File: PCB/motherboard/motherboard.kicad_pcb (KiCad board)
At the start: 2 copper layers, 68 parts, among them U1 TPS54140ADGQR, U2 PTPS259830LNRGER, U3 AP2112K-3.3TRG1, U4 NUCLEO-L432KC, U5 TXS0104EPWR, U6 LM74700QDBVTQ1, U7 25LC256-I/SN, U8 AM26LS32ACDR, U9 TL431D

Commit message: added last footprint on sch
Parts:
- added C26: DNP, Capacitor_SMD:C_1206_3216Metric_Pad1.33x1.80mm_HandSolder, F.Cu at (139.1, 117.9)
- added C27: 100n, Capacitor_SMD:C_1206_3216Metric_Pad1.33x1.80mm_HandSolder, F.Cu at (172.9, 46.7)
- added C28: 100n, Capacitor_SMD:C_1206_3216Metric_Pad1.33x1.80mm_HandSolder, F.Cu at (172.9, 50.0)
- added C29: 100n, Capacitor_SMD:C_1206_3216Metric_Pad1.33x1.80mm_HandSolder, F.Cu at (172.9, 53.4)
- added C30: 100n, Capacitor_SMD:C_1206_3216Metric_Pad1.33x1.80mm_HandSolder, F.Cu at (172.9, 56.7)
- added C31: 100n, Capacitor_SMD:C_1206_3216Metric_Pad1.33x1.80mm_HandSolder, F.Cu at (172.9, 60.1)
- added C32: 100n, Capacitor_SMD:C_1206_3216Metric_Pad1.33x1.80mm_HandSolder, F.Cu at (172.9, 63.4)
- added D1: 26V, diodes:SMB_L4.3-W3.6-LS5.4-BI, F.Cu at (146.5, 137.1)
- added J1: Conn_01x04, TerminalBlock_Phoenix:TerminalBlock_Phoenix_MPT-0,5-4-2.54_1x04_P2.54mm_Horizontal, F.Cu at (111.9, 127.3)
- added J10: Screw_Terminal_01x03, TerminalBlock_Phoenix:TerminalBlock_Phoenix_MPT-0,5-3-2.54_1x03_P2.54mm_Horizontal, F.Cu at (84.0, 128.0)
- added J11: Conn_01x05, TerminalBlock_Phoenix:TerminalBlock_Phoenix_MPT-0,5-5-2.54_1x05_P2.54mm_Horizontal, F.Cu at (94.2, 144.3)
- added J12: Conn_01x11, TerminalBlock_Phoenix:TerminalBlock_Phoenix_MPT-0,5-11-2.54_1x11_P2.54mm_Horizontal, F.Cu at (94.2, 110.3)
- added J13: Conn_01x03, TerminalBlock_Phoenix:TerminalBlock_Phoenix_MPT-0,5-3-2.54_1x03_P2.54mm_Horizontal, F.Cu at (84.0, 136.9)
- added J2: Conn_01x06, TerminalBlock_Phoenix:TerminalBlock_Phoenix_MPT-0,5-6-2.54_1x06_P2.54mm_Horizontal, F.Cu at (94.2, 127.3)
- added J3: Conn_01x08, TerminalBlock_Phoenix:TerminalBlock_Phoenix_MPT-0,5-8-2.54_1x08_P2.54mm_Horizontal, F.Cu at (94.2, 118.8)
- added J4: Conn_01x04, TerminalBlock_Phoenix:TerminalBlock_Phoenix_MPT-0,5-4-2.54_1x04_P2.54mm_Horizontal, F.Cu at (111.9, 135.8)
- added J5: Conn_01x03, TerminalBlock_Phoenix:TerminalBlock_Phoenix_MPT-0,5-3-2.54_1x03_P2.54mm_Horizontal, F.Cu at (84.0, 110.3)
- added J6: Conn_01x03, TerminalBlock_Phoenix:TerminalBlock_Phoenix_MPT-0,5-3-2.54_1x03_P2.54mm_Horizontal, F.Cu at (84.0, 119.2)
- added J8: Conn_01x06, TerminalBlock_Phoenix:TerminalBlock_Phoenix_MPT-0,5-6-2.54_1x06_P2.54mm_Horizontal, F.Cu at (94.2, 135.8)
- added J9: Conn_01x02, TerminalBlock_Phoenix:TerminalBlock_Phoenix_MKDS-3-2-5.08_1x02_P5.08mm_Horizontal, F.Cu at (110.4, 147.1)
- added L1: 47u, inductors:IND-SMD_L7.3-W6.8, F.Cu at (147.1, 130.2)
- added L2: 22uH, inductors:IND-SMD_L17.0-W17.0_YSPIA1770-100M, F.Cu at (92.2, 54.3)
- added L3: 22uH, inductors:IND-SMD_L17.0-W17.0_YSPIA1770-100M, F.Cu at (92.2, 72.9)
- added L4: 22uH, inductors:IND-SMD_L17.0-W17.0_YSPIA1770-100M, F.Cu at (92.2, 91.6)
- added Q1: NMOS, transistors:PG-TDSON-8_L5.0-W6.0-P1.27-BL-EP, F.Cu at (133.1, 88.5)
- added Q2: PMOS, transistors:DFN-8_L5.7-W4.9-P1.27-LS6.1-BL, F.Cu at (140.2, 88.4)
- added Q3: NMOS, transistors:SOT-23-3_L2.9-W1.3-P1.90-LS2.4-BR, F.Cu at (172.3, 92.1)
- added R28: 25 Ohm, resistors:TO-220-2_L10.1-W4.5-P5.08-L, F.Cu at (135.6, 80.7)
- added R29: 105k, Resistor_SMD:R_1206_3216Metric_Pad1.30x1.75mm_HandSolder, F.Cu at (157.0, 117.7)
- added R30: 6k49, Resistor_SMD:R_1206_3216Metric_Pad1.30x1.75mm_HandSolder, F.Cu at (157.0, 121.1)
- added R31: 10k, Resistor_SMD:R_1206_3216Metric_Pad1.30x1.75mm_HandSolder, F.Cu at (178.9, 59.9)
- C13: value C -> 3n9
- C6: value C -> 4n3
- C7: value C -> 220p
- D2: footprint Diode_SMD:D_SMA -> diodes:SMA_L4.4-W2.8-LS5.4-RD
- R11, R13, R15: value 15k -> 10k
- R14: value 100k -> 10k
- R2: value R -> 499k
- R22: value 4.7k -> 4k75
- R23: value 96k -> 95k3
- R3: value R -> 61k9
- R4: value R -> 27k4
- R5: value R -> 154
- R6: value R -> 1k4
- U9: footprint Package_SO:SOIC-8_3.9x4.9mm_P1.27mm -> diodes:SOT-23-3_L2.9-W1.5-P1.90-LS2.6-BR
- moved R13 95.9 mm to (157.0, 107.8)
- moved R14 95.9 mm to (157.0, 111.1)
- moved R15 95.9 mm to (157.0, 114.4)
- moved R10 95.1 mm to (151.0, 117.7)
- moved R7 95.1 mm to (151.0, 107.8)
- moved R8 95.1 mm to (151.0, 111.1)
- moved R9 95.1 mm to (151.0, 114.4)
- moved R1 94.3 mm to (145.1, 107.8)
- moved R2 94.3 mm to (145.1, 111.1)
- moved R3 94.3 mm to (145.1, 114.4)
- moved R4 94.3 mm to (145.1, 117.7)
- moved R5 94.3 mm to (145.1, 121.1)
- moved R11 86.4 mm to (151.0, 121.1)
- moved R12 86.4 mm to (151.0, 124.4)
- moved R6 86.2 mm to (145.1, 124.4)
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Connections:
- U2 pad 11: GND -> Net-(U2-NRETRY)
- U4 pad CN4_5: /CONNECTORS/PA2 -> /MCU+EEPROM/HEATER

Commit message: pcb layout
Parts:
- added D7: LED_YELLOW, LED_SMD:LED_1206_3216Metric_Pad1.42x1.75mm_HandSolder, F.Cu at (218.8, 116.0)
- added H1: MountingHole, MountingHole:MountingHole_3.2mm_M3, F.Cu at (101.4, 27.2)
- added H2: MountingHole, MountingHole:MountingHole_3.2mm_M3, F.Cu at (243.0, 27.2)
- added H3: MountingHole, MountingHole:MountingHole_3.2mm_M3, F.Cu at (243.0, 120.0)
- added H4: MountingHole, MountingHole:MountingHole_3.2mm_M3, F.Cu at (101.4, 120.0)
- added R32: 1k, Resistor_SMD:R_1206_3216Metric_Pad1.30x1.75mm_HandSolder, F.Cu at (222.8, 108.4)
- C3: footprint Capacitor_SMD:C_1206_3216Metric_Pad1.33x1.80mm_HandSolder -> Capacitor_SMD:C_Elec_10x10.2
- L1: footprint inductors:IND-SMD_L7.3-W6.8 -> inductors:IND-SMD_L13.5-W12.6_125CDMCC-DS
- U9: value TL431D -> TL431AIDR; footprint diodes:SOT-23-3_L2.9-W1.5-P1.90-LS2.6-BR -> TL431AIDR:D8
- moved J10 175.4 mm to (227.9, 27.6), turned to 180 degrees
- moved J11 154.0 mm to (194.3, 27.4), turned to 180 degrees
- moved L4 149.4 mm to (236.2, 51.8), turned to 90 degrees
- moved J9 142.8 mm to (240.6, 88.4), turned to 90 degrees
- moved C18 141.2 mm to (237.6, 38.4), turned to 90 degrees
- moved C15 141.1 mm to (241.0, 38.4), turned to 90 degrees
- moved R16 128.9 mm to (234.2, 38.4), turned to -90 degrees
- moved L2 123.7 mm to (215.8, 51.8), turned to 90 degrees
- moved J3 122.1 mm to (175.1, 27.4), turned to 180 degrees
- moved C19 120.8 mm to (214.0, 38.6), turned to 90 degrees
- moved R17 114.3 mm to (217.4, 38.6), turned to -90 degrees
- moved C16 113.5 mm to (210.6, 38.6), turned to 90 degrees
- moved C3 111.7 mm to (231.2, 74.2), turned to 90 degrees
- moved C20 104.9 mm to (193.8, 38.6), turned to 90 degrees
- moved L3 104.4 mm to (194.4, 51.8), turned to 90 degrees
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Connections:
- J9 pad 1: +24V -> +24V_UNPROTECTED
- U5 pad 6: (no net) -> unconnected-(U5-NC-Pad6)
- U5 pad 9: (no net) -> unconnected-(U5-NC-Pad9)
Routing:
- net /CONNECTORS/ESCON_A_IN_1: track 0.00 -> 40.0 mm
- net /CONNECTORS/ESCON_A_IN_1\: track 0.00 -> 37.5 mm
- net /CONNECTORS/ESCON_A_IN_2: track 0.00 -> 35.0 mm
- net /CONNECTORS/ESCON_A_IN_2\: track 0.00 -> 33.4 mm
- net /CONNECTORS/ESCON_A_OUT_1: track 0.00 -> 31.8 mm
- net /CONNECTORS/ESCON_A_OUT_2: track 0.00 -> 30.2 mm
- net /CONNECTORS/ESCON_D_IN_1: track 0.00 -> 28.8 mm
- net Net-(U2-OVLO): track 0.00 -> 27.9 mm
- net /CONNECTORS/ESCON_D_IN_2: track 0.00 -> 27.5 mm
- net /CONNECTORS/ESCON_D_IO_3: track 0.00 -> 26.4 mm
- net /CONNECTORS/ESCON_D_IO_4: track 0.00 -> 23.4 mm
- net Net-(U1-COMP): track 0.00 -> 21.5 mm
- net /CONNECTORS/H1: track 0.00 -> 21.4 mm
- net /CONNECTORS/ENC_A: track 0.00 -> 19.6 mm
- net /CONNECTORS/H2: track 0.00 -> 17.8 mm
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- added copper zone on F.Cu, net +24V
- added copper zone on F.Cu, net +24V_ESCON
- added copper zone on F.Cu, net +24V_UNPROTECTED
- added copper zone on F.Cu, net +3.3V
- added copper zone on F.Cu, net +5V
- added copper zone on F.Cu, net /ESCON 50_5+PROTECTION/MW1
- added copper zone on F.Cu, net /ESCON 50_5+PROTECTION/MW2
- added copper zone on F.Cu, net /ESCON 50_5+PROTECTION/MW3
- added copper zone on F.Cu, net Net-(D2-K)
- added copper zone on F.Cu, net Net-(Q2-D)
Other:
- board outline added: 148.8 x 100 mm
- copper layers 2 -> 4

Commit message: pcb layout : collegamento piste + vie + cambio connettori
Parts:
- J10: footprint TerminalBlock_Phoenix:TerminalBlock_Phoenix_MPT-0,5-3-2.54_1x03_P2.54mm_Horizontal -> TerminalBlock_Phoenix:TerminalBlock_Phoenix_PT-1,5-3-5.0-H_1x03_P5.00mm_Horizontal
- J4: footprint TerminalBlock_Phoenix:TerminalBlock_Phoenix_MPT-0,5-4-2.54_1x04_P2.54mm_Horizontal -> Connector_PinSocket_2.54mm:PinSocket_1x04_P2.54mm_Vertical
- moved C30 40.5 mm to (137.2, 114.8), turned to 0 degrees
- moved Q3 40.4 mm to (141.4, 93.2), turned to 90 degrees
- moved R31 34.2 mm to (136.2, 94.0), turned to -90 degrees
- moved C31 32.6 mm to (137.2, 89.6), turned to 0 degrees
- moved J5 16.5 mm to (149.2, 120.0)
- moved C29 13.9 mm to (118.0, 54.0), turned to 180 degrees
- moved R19 11.1 mm to (124.2, 70.5), turned to 0 degrees
- moved J6 10.7 mm to (164.2, 120.0)
- moved R20 9.71 mm to (155.4, 111.8)
- moved U7 9.71 mm to (153.0, 105.8)
- moved R21 9.71 mm to (149.6, 111.8)
- moved C32 9.71 mm to (149.6, 100.2)
- moved R25 9.71 mm to (155.6, 100.2)
- moved J12 7.90 mm to (136.5, 27.4)
- moved U5 7.63 mm to (122.9, 65.2)
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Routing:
- net /MCU+EEPROM/IMON_EFUSE: track 13.1 -> 126.8 mm, vias 0 -> 1
- net /MCU+EEPROM/SPI_MISO: track 0.00 -> 95.2 mm, vias 0 -> 2
- net /MCU+EEPROM/SPI_SCK: track 0.00 -> 91.9 mm, vias 0 -> 2
- net /MCU+EEPROM/SPI_MOSI: track 0.00 -> 90.8 mm, vias 0 -> 2
- net /CONNECTORS/ESCON_D_IN_1: track 28.8 -> 119.7 mm, vias 0 -> 1
- net /CONNECTORS/ESCON_D_IO_3: track 26.4 -> 113.8 mm, vias 0 -> 1
- net /CONNECTORS/ESCON_D_IO_4: track 23.4 -> 104.5 mm, vias 0 -> 1
- net /CONNECTORS/ESCON_D_IN_2: track 27.5 -> 107.8 mm, vias 0 -> 1
- net /CONNECTORS/HEAT_GND: track 0.00 -> 72.5 mm, vias 0 -> 1
- net /CONNECTORS/SDA: track 0.00 -> 68.1 mm
- net /CONNECTORS/SCL: track 0.00 -> 64.3 mm, vias 0 -> 1
- net /CONNECTORS/ENC_B: track 16.6 -> 79.5 mm, vias 0 -> 1
- net /CONNECTORS/ENC_Z: track 0.00 -> 55.9 mm, vias 0 -> 1
- net /MCU+EEPROM/ENC_A_SE: track 0.00 -> 52.9 mm, vias 0 -> 1
- net /CONNECTORS/ENC_B\: track 13.0 -> 65.8 mm, vias 0 -> 1
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
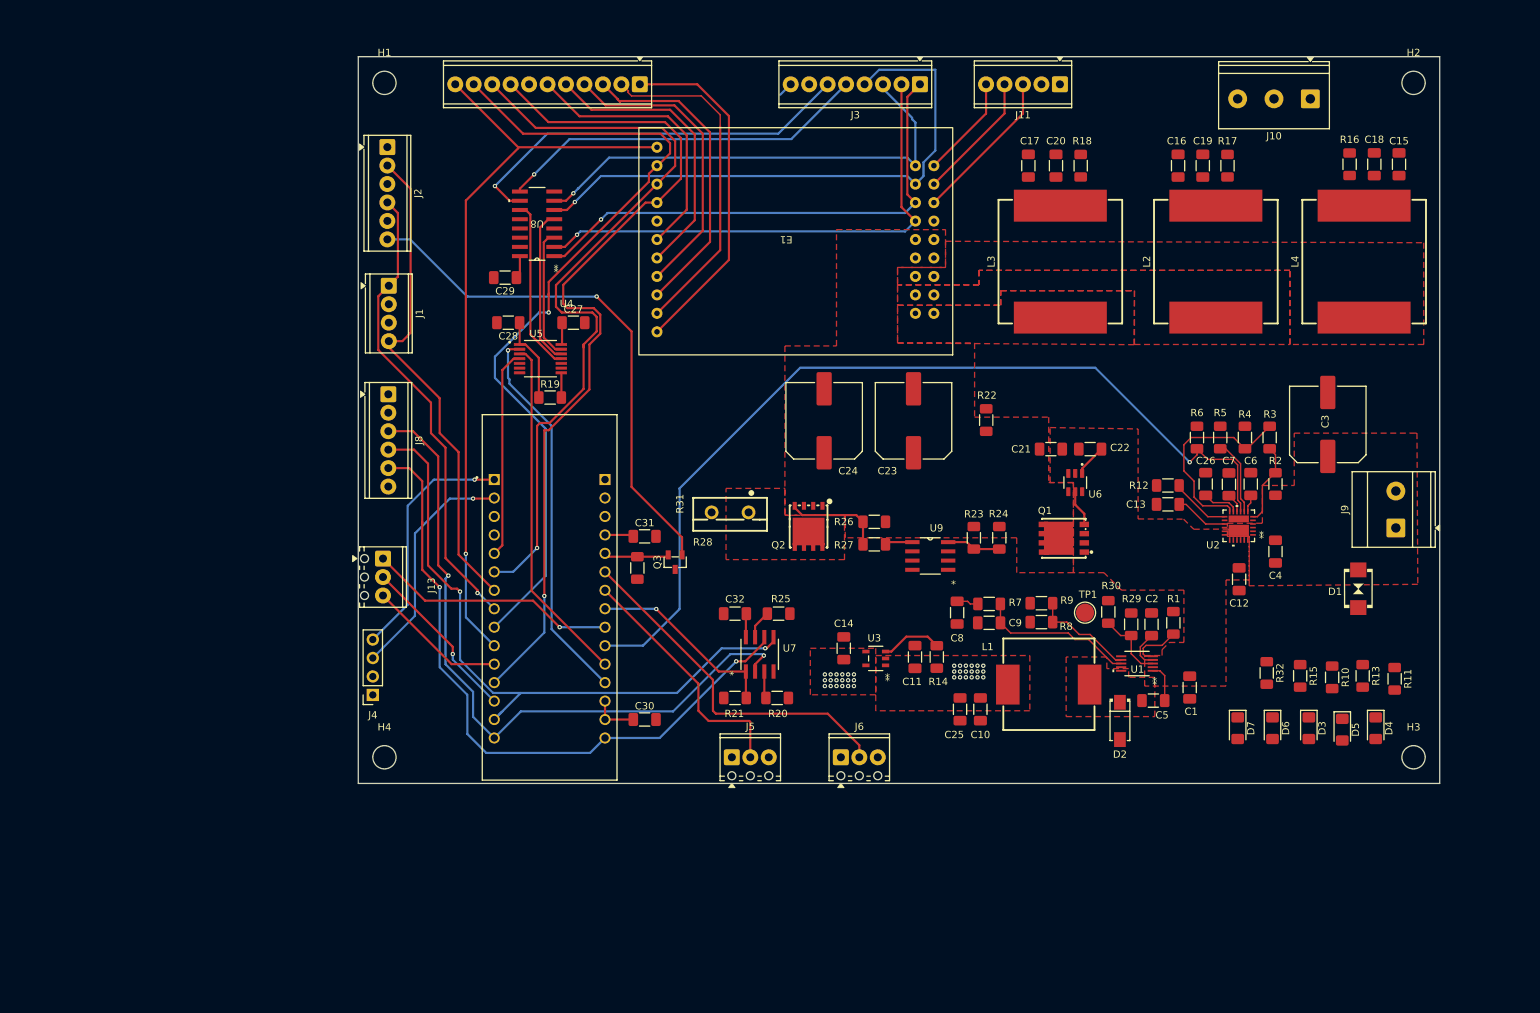
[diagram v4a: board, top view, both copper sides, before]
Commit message: resolved pcb errors from drc, generated test output files
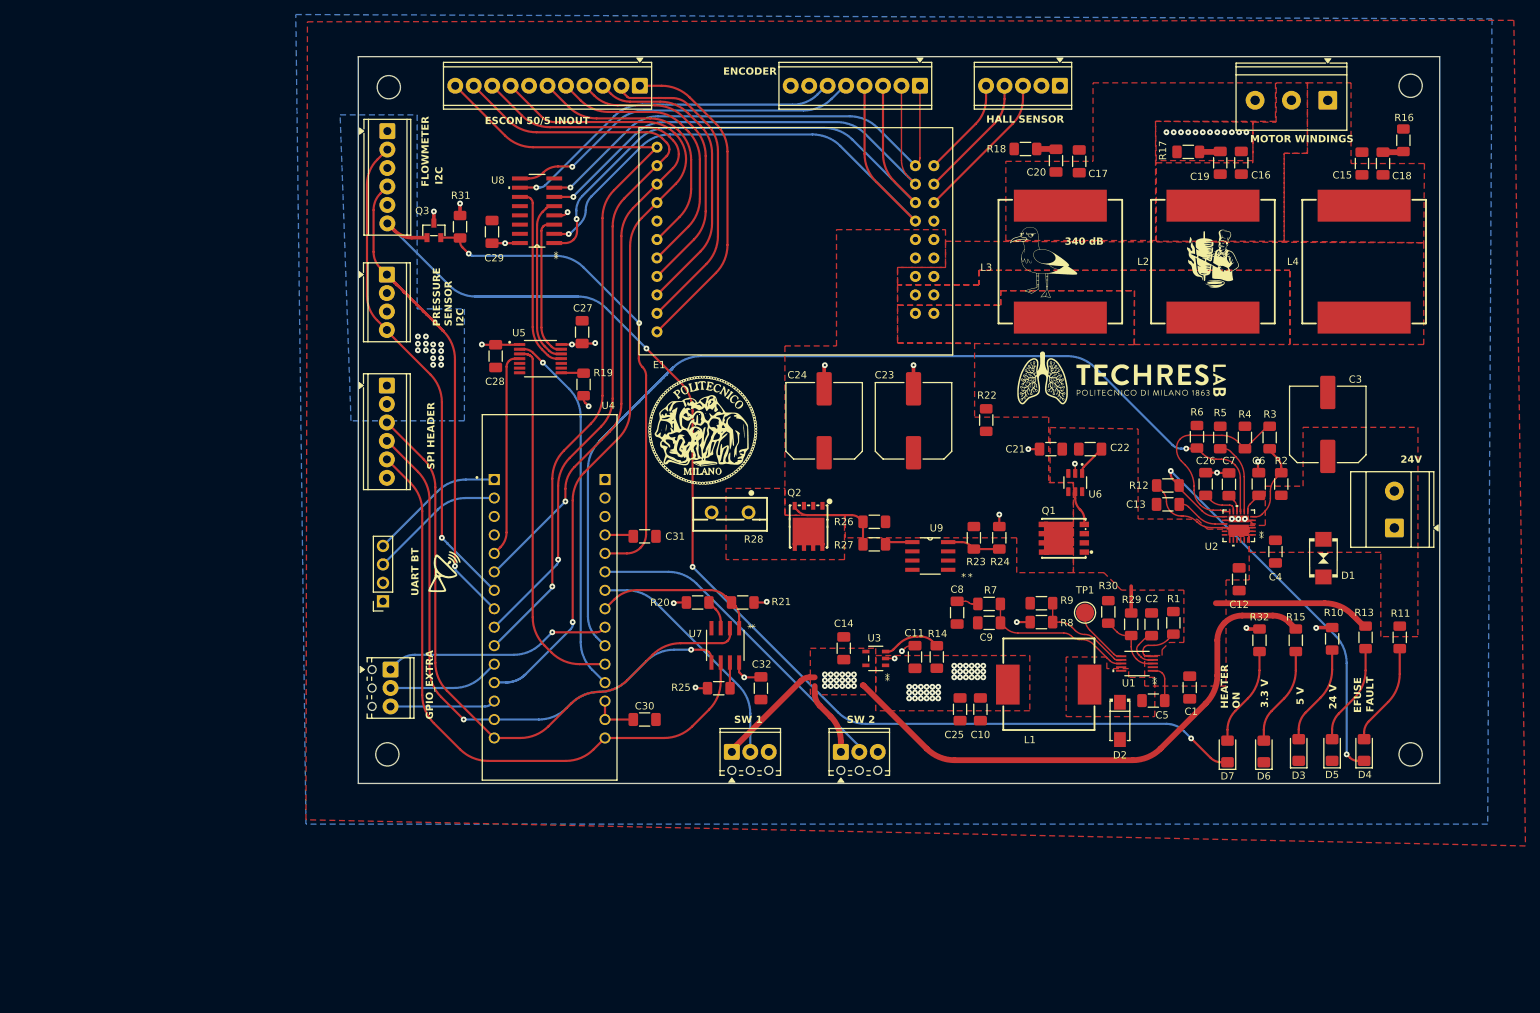
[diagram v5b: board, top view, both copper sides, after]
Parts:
- added G***: LOGO, LOGO, F.Cu at (145.2, 75.0)
- added G***: LOGO, LOGO, F.Cu at (215.4, 51.3)
- added G***: LOGO, LOGO, F.Cu at (203.0, 67.8)
- added G***: LOGO, LOGO, F.Cu at (192.1, 52.1)
- added G***: LOGO, LOGO, F.Cu at (109.8, 94.8)
- added G***: LOGO, LOGO, B.Cu at (219.1, 115.7)
- moved Q3 56.4 mm to (108.2, 47.5), turned to -90 degrees
- moved R31 52.9 mm to (111.8, 47.0), turned to 90 degrees
- moved R20 17.1 mm to (144.5, 98.7), turned to 0 degrees
- moved J13 15.3 mm to (102.2, 107.9)
- moved R21 13.2 mm to (150.7, 98.7), turned to 180 degrees
- moved R25 13.2 mm to (147.4, 110.5), turned to 0 degrees
- moved J4 13.0 mm to (101.2, 98.5)
- moved C32 10.9 mm to (153.2, 110.5), turned to -90 degrees
- moved C16 8.71 mm to (219.3, 38.2)
- moved R16 8.10 mm to (241.6, 35.1), turned to 90 degrees
- moved R18 7.94 mm to (189.6, 36.3), turned to 180 degrees
- moved C17 7.03 mm to (197.0, 38.0)
- moved C29 6.55 mm to (116.2, 47.7), turned to 90 degrees
- moved D1 6.38 mm to (230.6, 92.6)
- moved R11 5.74 mm to (241.1, 103.5), turned to 90 degrees
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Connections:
- J10 pad 1: /CONNECTORS/MW1_motor -> /CONNECTORS/MW3_motor
- J10 pad 3: /CONNECTORS/MW3_motor -> /CONNECTORS/MW1_motor
- J13 pad 2: /CONNECTORS/PA11 -> /CONNECTORS/PC15
- J13 pad 3: /CONNECTORS/PC15 -> /CONNECTORS/PA11
- J3 pad 1: /CONNECTORS/ENC_A\ -> /CONNECTORS/ENC_B\
- J3 pad 2: /CONNECTORS/ENC_A -> /CONNECTORS/ENC_B
- J3 pad 3: /CONNECTORS/ENC_B\ -> /CONNECTORS/ENC_A\
- J3 pad 4: /CONNECTORS/ENC_B -> /CONNECTORS/ENC_A
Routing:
- net +3.3V: track 15.1 -> 120.4 mm, vias 18 -> 38
- net /CONNECTORS/HEAT_GND: track 72.5 -> 165.0 mm, vias 1 -> 3
- net /MCU+EEPROM/HEATER: track 8.99 -> 68.9 mm, vias 0 -> 2
- net Net-(D4-K): track 8.24 -> 61.9 mm, vias 0 -> 2
- net GND: track 0.00 -> 27.6 mm, vias 0 -> 26
- net +24V: track 0.00 -> 25.3 mm
- net +24V_UNPROTECTED: track 0.00 -> 20.6 mm
- net /CONNECTORS/HC_RX: track 33.8 -> 18.9 mm, vias 1 -> 0
- net Net-(D4-A): track 0.00 -> 14.1 mm
- net Net-(D5-A): track 0.00 -> 14.0 mm
- net Net-(D3-A): track 0.00 -> 13.7 mm
- net Net-(D7-A): track 0.00 -> 13.6 mm
- net Net-(D6-A): track 0.00 -> 13.6 mm
- net /CONNECTORS/HC_TX: track 32.5 -> 18.9 mm, vias 1 -> 0
- net /CONNECTORS/ENC_A: track 70.9 -> 82.3 mm
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- added copper zone on B.Cu, net +3.3V
- added copper zone on In2.Cu, net +3.3V
- added copper zone on In2.Cu, net +5V
- added copper zone on F.Cu, net /CONNECTORS/MW1_motor
- added copper zone on F.Cu, net /CONNECTORS/MW2_motor
- added copper zone on F.Cu, net /CONNECTORS/MW3_motor
- added copper zone on B.Cu, net GND
- added copper zone on F.Cu, net GND
- added copper zone on In1.Cu, net GND
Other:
- board text added: "(1. TOGLIERSI LE CIABATTE) 2. COLLEGARE LA SCHEDA A 24V 3. UTILIZZARE LA SCHEDA"
- board text added: "24 V"
- board text added: "24V"
- board text added: "3.3 V"
- board text added: "3.3V"
- board text added: "340 dB"
- board text added: "5 V"
- board text added: "5V"
- board text added: "A_IN_1 +"
- board text added: "A_IN_1 -"
- board text added: "A_IN_2 +"
- board text added: "A_IN_2 -"
- board text added: "A_OUT_1"
- board text added: "A_OUT_2"
- board text added: "Board No."
- board text added: "D_IN_1"
- board text added: "D_IN_2"
- board text added: "D_IO_3"
- board text added: "D_IO_4"
- board text added: "EFUSE"
- board text added: "ENCODER"
- board text added: "ENC_A +"
- board text added: "ENC_A -"
- board text added: "ENC_B +"
- board text added: "ENC_B -"
- board text added: "ENC_Z +"
- board text added: "ENC_Z -"
- board text added: "ESCON 50/5 INOUT"
- board text added: "FAULT"
- board text added: "FLOWMETER"
- board text added: "FRANCESCO SIMONE ANDREA CHRISTIAN MARTINA"
- board text added: "GND"
- board text added: "GPIO_EXTRA"
- board text added: "H1"
- board text added: "H2"
- board text added: "H3"
- board text added: "HALL SENSOR"
- board text added: "HC_RX"
- board text added: "HC_TX"
- board text added: "HEATER ON"
- board text added: "HEAT_GND"
- board text added: "I2C"
- board text added: "ISTRUZIONI D'USO :"
- board text added: "MADE IN POLIMI BY GRUPPO VIOLA (VETERANI DEL SALTO)"
- board text added: "MISO"
- board text added: "MOSI"
- board text added: "MOTOR WINDINGS"
- board text added: "MW1"
- board text added: "MW2"
- board text added: "MW3"
- board text added: "PA11"
- board text added: "PA3"
- board text added: "PC15"
- board text added: "PRESSURE SENSOR I2C"
- board text added: "SCK"
- board text added: "SCL"
- board text added: "SDA"
- board text added: "SPI HEADER"
- board text added: "SW 1"
- board text added: "SW 2"
- board text added: "SW_1"
- board text added: "SW_2"
- board text added: "UART BT"
